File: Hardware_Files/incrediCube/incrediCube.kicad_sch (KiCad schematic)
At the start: 0 parts

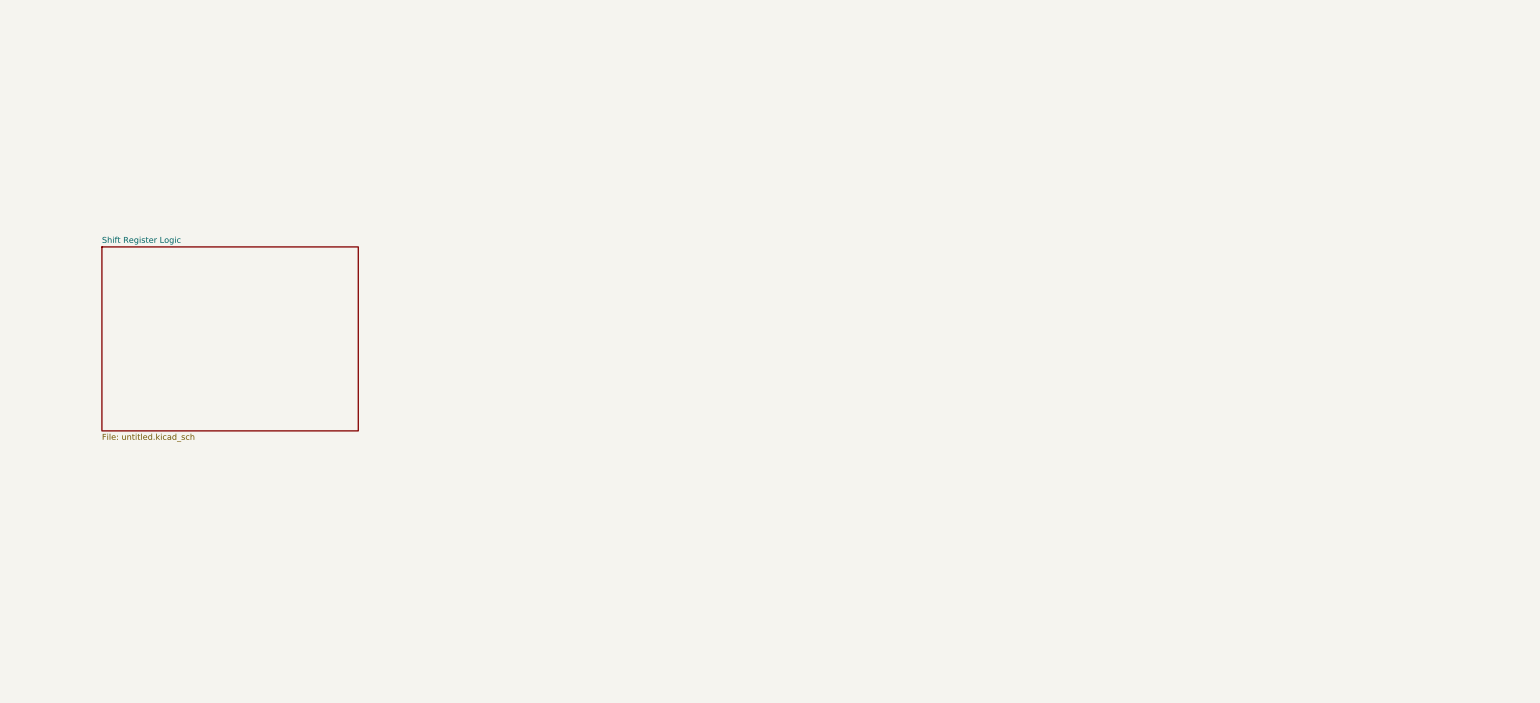
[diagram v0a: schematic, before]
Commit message: LED Grids
Added to KiCAD schematic, plus MOSFETs.
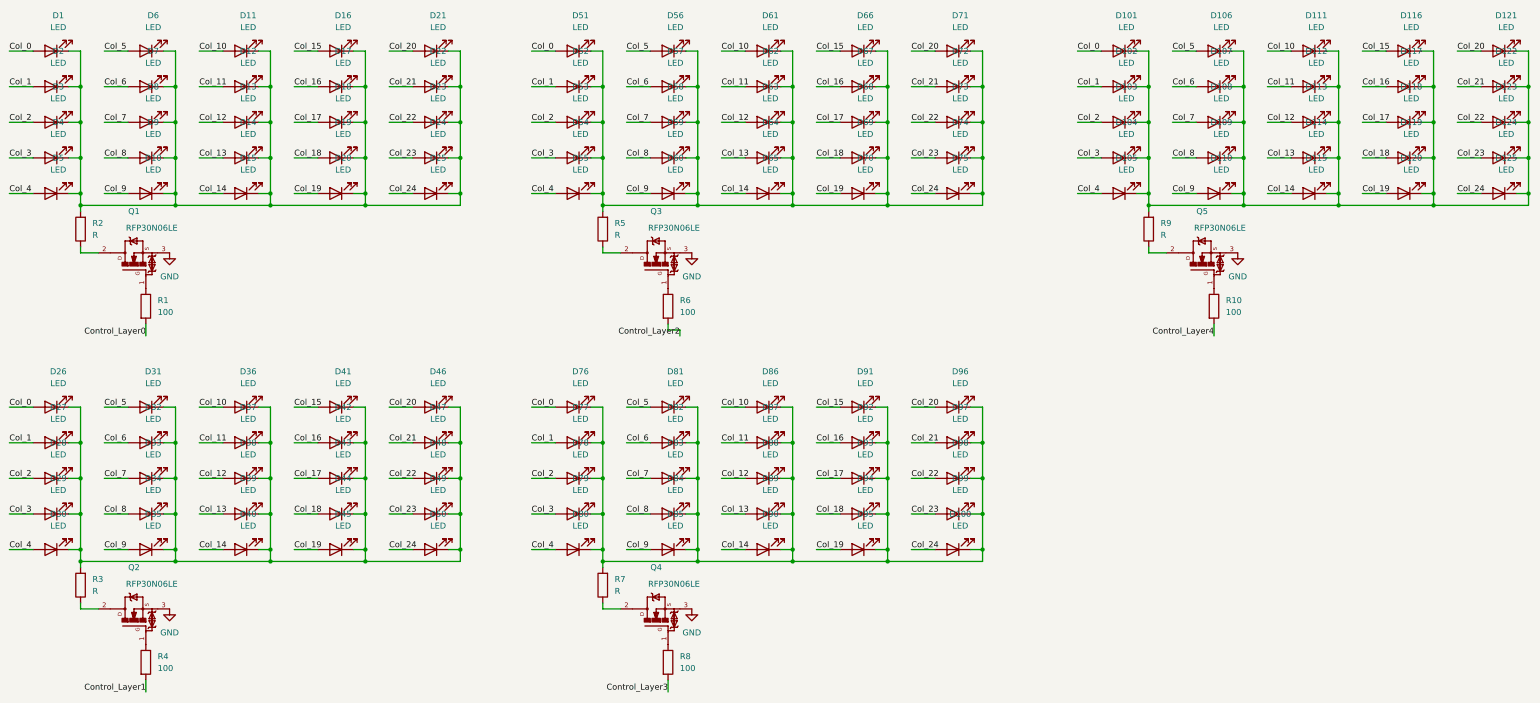
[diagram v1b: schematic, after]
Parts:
- added D1, D10, D100, D101, D102, D103, D104, D105, D106, D107, D108, D109, D11, D110, D111, D112, D113, D114, D115, D116, D117, D118, D119, D12, D120, D121, D122, D123, D124, D125, D13, D14, D15, D16, D17, D18, D19, D2, D20, D21, D22, D23, D24, D25, D26, D27, D28, D29, D3, D30, D31, D32, D33, D34, D35, D36, D37, D38, D39, D4, D40, D41, D42, D43, D44, D45, D46, D47, D48, D49, D5, D50, D51, D52, D53, D54, D55, D56, D57, D58, D59, D6, D60, D61, D62, D63, D64, D65, D66, D67, D68, D69, D7, D70, D71, D72, D73, D74, D75, D76, D77, D78, D79, D8, D80, D81, D82, D83, D84, D85, D86, D87, D88, D89, D9, D90, D91, D92, D93, D94, D95, D96, D97, D98, D99: LED, symbol Device:LED
- added Q1, Q2, Q3, Q4, Q5: RFP30N06LE, MOSFETs:TRANS_RFP30N06LE, symbol MOSFETs:RFP30N06LE
- added R1, R10, R4, R6, R8: 100, symbol Device:R
- added R2, R3, R5, R7, R9: R, symbol Device:R
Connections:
- new net: D1.1 (K), D10.1 (K), D11.1 (K), D12.1 (K), D13.1 (K), D14.1 (K), D15.1 (K), D16.1 (K), D17.1 (K), D18.1 (K), D19.1 (K), D2.1 (K), D20.1 (K), D21.1 (K), D22.1 (K), D23.1 (K), D24.1 (K), D25.1 (K), D3.1 (K), D4.1 (K), D5.1 (K), D6.1 (K), D7.1 (K), D8.1 (K), D9.1 (K), R2.2
- new net: Q3.1, R6.1
- new net: Q3.2, R5.1
- new net: D26.1 (K), D27.1 (K), D28.1 (K), D29.1 (K), D30.1 (K), D31.1 (K), D32.1 (K), D33.1 (K), D34.1 (K), D35.1 (K), D36.1 (K), D37.1 (K), D38.1 (K), D39.1 (K), D40.1 (K), D41.1 (K), D42.1 (K), D43.1 (K), D44.1 (K), D45.1 (K), D46.1 (K), D47.1 (K), D48.1 (K), D49.1 (K), D50.1 (K), R3.2
- new net: D100.1 (K), D76.1 (K), D77.1 (K), D78.1 (K), D79.1 (K), D80.1 (K), D81.1 (K), D82.1 (K), D83.1 (K), D84.1 (K), D85.1 (K), D86.1 (K), D87.1 (K), D88.1 (K), D89.1 (K), D90.1 (K), D91.1 (K), D92.1 (K), D93.1 (K), D94.1 (K), D95.1 (K), D96.1 (K), D97.1 (K), D98.1 (K), D99.1 (K), R7.2
- new net: D51.1 (K), D52.1 (K), D53.1 (K), D54.1 (K), D55.1 (K), D56.1 (K), D57.1 (K), D58.1 (K), D59.1 (K), D60.1 (K), D61.1 (K), D62.1 (K), D63.1 (K), D64.1 (K), D65.1 (K), D66.1 (K), D67.1 (K), D68.1 (K), D69.1 (K), D70.1 (K), D71.1 (K), D72.1 (K), D73.1 (K), D74.1 (K), D75.1 (K), R5.2
- new net: D101.1 (K), D102.1 (K), D103.1 (K), D104.1 (K), D105.1 (K), D106.1 (K), D107.1 (K), D108.1 (K), D109.1 (K), D110.1 (K), D111.1 (K), D112.1 (K), D113.1 (K), D114.1 (K), D115.1 (K), D116.1 (K), D117.1 (K), D118.1 (K), D119.1 (K), D120.1 (K), D121.1 (K), D122.1 (K), D123.1 (K), D124.1 (K), D125.1 (K), R9.2
- new net: Q2.1, R4.1
- new net: Q4.1, R8.1
- new net: Q1.1, R1.1
- new net: Q1.2, R2.1
- new net: Q2.2, R3.1
- new net: Q5.1, R10.1
- new net: Q5.2, R9.1
- new net: Q4.2, R7.1
- new net Col_0: D1.2 (A), D101.2 (A), D26.2 (A), D51.2 (A), D76.2 (A)
- new net Col_1: D102.2 (A), D2.2 (A), D27.2 (A), D52.2 (A), D77.2 (A)
- new net Col_10: D11.2 (A), D111.2 (A), D36.2 (A), D61.2 (A), D86.2 (A)
- new net Col_11: D112.2 (A), D12.2 (A), D37.2 (A), D62.2 (A), D87.2 (A)
- new net Col_12: D113.2 (A), D13.2 (A), D38.2 (A), D63.2 (A), D88.2 (A)
- new net Col_13: D114.2 (A), D14.2 (A), D39.2 (A), D64.2 (A), D89.2 (A)
- new net Col_14: D115.2 (A), D15.2 (A), D40.2 (A), D65.2 (A), D90.2 (A)
- new net Col_15: D116.2 (A), D16.2 (A), D41.2 (A), D66.2 (A), D91.2 (A)
- new net Col_16: D117.2 (A), D17.2 (A), D42.2 (A), D67.2 (A), D92.2 (A)
- new net Col_17: D118.2 (A), D18.2 (A), D43.2 (A), D68.2 (A), D93.2 (A)
- new net Col_18: D119.2 (A), D19.2 (A), D44.2 (A), D69.2 (A), D94.2 (A)
- new net Col_19: D120.2 (A), D20.2 (A), D45.2 (A), D70.2 (A), D95.2 (A)
- new net Col_2: D103.2 (A), D28.2 (A), D3.2 (A), D53.2 (A), D78.2 (A)
- new net Col_20: D121.2 (A), D21.2 (A), D46.2 (A), D71.2 (A), D96.2 (A)
- new net Col_21: D122.2 (A), D22.2 (A), D47.2 (A), D72.2 (A), D97.2 (A)
- new net Col_22: D123.2 (A), D23.2 (A), D48.2 (A), D73.2 (A), D98.2 (A)
- new net Col_23: D124.2 (A), D24.2 (A), D49.2 (A), D74.2 (A), D99.2 (A)
- new net Col_24: D100.2 (A), D125.2 (A), D25.2 (A), D50.2 (A), D75.2 (A)
- new net Col_3: D104.2 (A), D29.2 (A), D4.2 (A), D54.2 (A), D79.2 (A)
- new net Col_4: D105.2 (A), D30.2 (A), D5.2 (A), D55.2 (A), D80.2 (A)
- new net Col_5: D106.2 (A), D31.2 (A), D56.2 (A), D6.2 (A), D81.2 (A)
- new net Col_6: D107.2 (A), D32.2 (A), D57.2 (A), D7.2 (A), D82.2 (A)
- new net Col_7: D108.2 (A), D33.2 (A), D58.2 (A), D8.2 (A), D83.2 (A)
- new net Col_8: D109.2 (A), D34.2 (A), D59.2 (A), D84.2 (A), D9.2 (A)
- new net Col_9: D10.2 (A), D110.2 (A), D35.2 (A), D60.2 (A), D85.2 (A)
- new net Control_Layer0: R1.2
- new net Control_Layer1: R4.2
- new net Control_Layer2: R6.2
- new net Control_Layer3: R8.2
- new net Control_Layer4: R10.2
- new net GND: Q1.3, Q2.3, Q3.3, Q4.3, Q5.3
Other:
- removed sheet Shift Register Logic
- company: (none) -> ECE230 Michael Fang | Chase Robinson
- title: (none) -> incrediCube
